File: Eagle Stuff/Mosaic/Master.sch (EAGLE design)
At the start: 9 parts

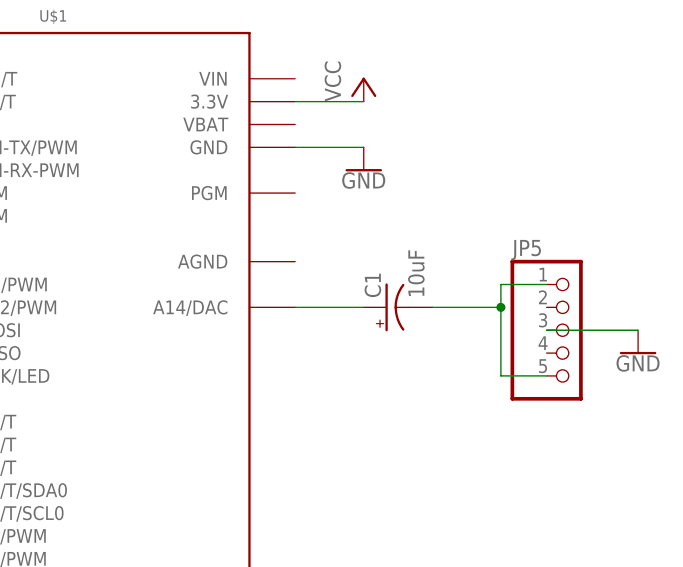
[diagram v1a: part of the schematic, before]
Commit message: Fixed capacitor drill hole diameter
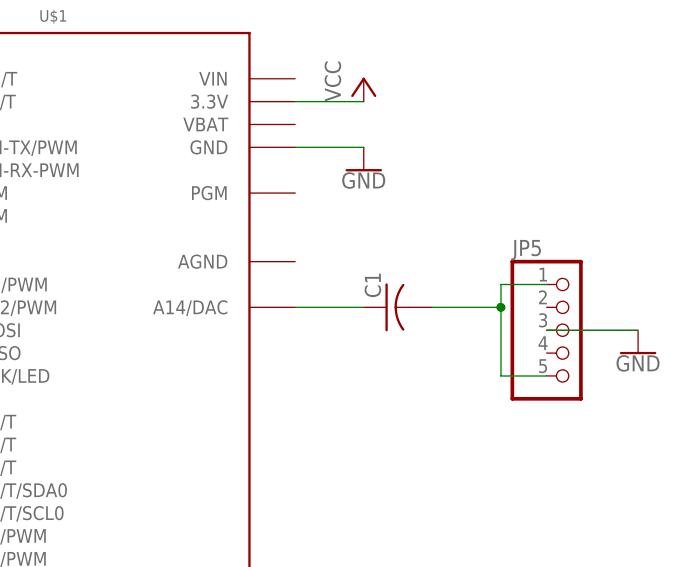
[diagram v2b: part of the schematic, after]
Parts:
- C1: value 10uF -> (none); device SparkFun-Capacitors:10UF-POLAR-RADIAL-2.5MM-25V-20% -> rcl:C-US025-030X050
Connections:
- net N$3: now also C1.1; no longer C1.+
- net N$4: now also C1.2; no longer C1.-
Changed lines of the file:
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@@
 <part name="U$1" library="Teensy_3_and_LC_Series_Boards_v1.4" deviceset="TEENSY_3.1-3.2_OUTER_ROW" device=""/>
 <part name="JP5" library="pinhead" deviceset="PINHD-1X5" device=""/>
-<part name="C1" library="SparkFun-Capacitors" deviceset="10UF-POLAR" device="-RADIAL-2.5MM-25V-20%" value="10uF"/>
 <part name="GND6" library="SparkFun-PowerSymbols" deviceset="GND" device=""/>
+<part name="C1" library="rcl" deviceset="C-US" device="025-030X050"/>
 </parts>
 <sheets>
@@
 <instance part="U$1" gate="G$1" x="12.7" y="50.8"/>
 <instance part="JP5" gate="A" x="66.04" y="50.8"/>
+<instance part="GND6" gate="1" x="73.66" y="48.26"/>
 <instance part="C1" gate="G$1" x="45.72" y="53.34" rot="R90"/>
-<instance part="GND6" gate="1" x="73.66" y="48.26"/>
 </instances>
 <busses>
@@
 <segment>
 <pinref part="U$1" gate="G$1" pin="A14/DAC"/>
-<pinref part="C1" gate="G$1" pin="+"/>
 <wire x1="35.56" y1="53.34" x2="43.18" y2="53.34" width="0.1524" layer="91"/>
+<pinref part="C1" gate="G$1" pin="1"/>
 </segment>
 </net>
 <net name="N$4" class="0">
 <segment>
-<pinref part="C1" gate="G$1" pin="-"/>
 <wire x1="50.8" y1="53.34" x2="58.42" y2="53.34" width="0.1524" layer="91"/>
 <wire x1="58.42" y1="53.34" x2="58.42" y2="55.88" width="0.1524" layer="91"/>
@@
 <wire x1="58.42" y1="45.72" x2="58.42" y2="53.34" width="0.1524" layer="91"/>
 <junction x="58.42" y="53.34"/>
+<pinref part="C1" gate="G$1" pin="2"/>
 </segment>
 </net>
